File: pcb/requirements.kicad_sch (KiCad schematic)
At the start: 4 parts

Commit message: Updated worksheet template and logo
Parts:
- removed LOGO1: ~, CRGM Logos:FNWW Face 10mm, symbol CRGM Logos:FNWW Face
- added LOGO1: ~, CRGM Logos:CRGM Logo 5mm, symbol CRGM Logos:CRGM Logo
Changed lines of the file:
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@@
+	)
+	(symbol
+		(lib_id "CRGM Logos:CRGM Logo")
+		(at 245.11 173.99 0)
+		(unit 1)
+		(exclude_from_sim no)
+		(in_bom yes)
+		(on_board yes)
+		(dnp no)
+		(property "Reference" "LOGO1"
+			(at 245.11 185.674 0)
+			(effects
+				(font
+					(size 1.27 1.27)
+				)
+				(hide yes)
+			)
+		)
+		(property "Value" "~"
+			(at 245.11 173.99 0)
+			(effects
+				(font
+					(size 1.27 1.27)
+				)
+			)
+		)
+		(property "Footprint" "CRGM Logos:CRGM Logo 5mm"
+			(at 245.11 187.452 0)
+			(effects
+				(font
+					(size 1.27 1.27)
+				)
+				(hide yes)
+			)
+		)
+		(property "Datasheet" ""
+			(at 245.11 173.99 0)
+			(effects
+				(font
+					(size 1.27 1.27)
+				)
+				(hide yes)
+			)
+		)
+		(property "Description" ""
+			(at 245.11 173.99 0)
+			(effects
+				(font
+					(size 1.27 1.27)
+				)
+				(hide yes)
+			)
+		)
+		(property "LCSC" ""
+			(at 245.11 173.99 0)
+			(effects
+				(font
+					(size 1.27 1.27)
+				)
+				(hide yes)
+			)
+		)
+		(property "Digikey" ""
+			(at 245.11 173.99 0)
+			(effects
+				(font
+					(size 1.27 1.27)
+				)
+				(hide yes)
+			)
+		)
+		(property "Mouser" ""
+			(at 245.11 173.99 0)
+			(effects
+				(font
+					(size 1.27 1.27)
+				)
+				(hide yes)
+			)
+		)
+		(instances
+			(project ""
+				(path "/39407804-2746-45a9-a901-1039a9921518/2e166321-b713-45e0-87cf-342f1811c390"
+					(reference "LOGO1")
+					(unit 1)
+				)
+			)
+		)
 	)
 	(symbol
@@
 					(unit 1)
 				)
-			)
-		)
-	)
-	(symbol
-		(lib_id "CRGM Logos:FNWW Face")
-		(at 246.38 173.99 0)
-		(unit 1)
-		(exclude_from_sim no)
-		(in_bom no)
-		(on_board yes)
-		(dnp no)
-		(fields_autoplaced yes)
-		(property "Reference" "LOGO1"
-			(at 246.38 175.006 0)
-			(effects
-				(font
-					(size 1.27 1.27)
-				)
-				(hide yes)
-			)
-		)
-		(property "Value" "~"
-			(at 243.84 169.164 0)
-			(effects
-				(font
-					(size 1.27 1.27)
-				)
-				(hide yes)
-			)
-		)
-		(property "Footprint" "CRGM Logos:FNWW Face 10mm"
-			(at 246.38 183.134 0)
-			(effects
-				(font
-					(size 1.27 1.27)
-				)
-				(hide yes)
-			)
-		)
-		(property "Datasheet" ""
-			(at 243.84 169.164 0)
-			(effects
-				(font
-					(size 1.27 1.27)
-				)
-				(hide yes)
-			)
-		)
-		(property "Description" ""
-			(at 243.84 169.164 0)
-			(effects
-				(font
-					(size 1.27 1.27)
-				)
-				(hide yes)
-			)
-		)
-		(property "LCSC" ""
-			(at 246.38 173.99 0)
-			(effects
-				(font
-					(size 1.27 1.27)
-				)
-				(hide yes)
-			)
-		)
-		(property "Digikey" ""
-			(at 246.38 173.99 0)
-			(effects
-				(font
-					(size 1.27 1.27)
-				)
-				(hide yes)
-			)
-		)
-		(property "Mouser" ""
-			(at 246.38 173.99 0)
-			(effects
-				(font
-					(size 1.27 1.27)
-				)
-				(hide yes)
-			)
-		)
-		(instances
-			(project ""
-				(path "/39407804-2746-45a9-a901-1039a9921518/2e166321-b713-45e0-87cf-342f1811c390"
-					(reference "LOGO1")
-					(unit 1)
-				)

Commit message: Fixed footprint for Buzzer, XFC, USB ESD, and Power Switcher
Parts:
- LOGO1: now left out of the parts list
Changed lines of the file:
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@@
 		(unit 1)
 		(exclude_from_sim no)
-		(in_bom yes)
+		(in_bom no)
 		(on_board yes)
 		(dnp no)

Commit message: Change name in schematic
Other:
- title: Node Hardware -> Hub Hardware
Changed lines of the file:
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@@
 	(paper "A4")
 	(title_block
-		(title "Node Hardware")
+		(title "Hub Hardware")
 		(date "<<release-date>>")
 		(rev "<<tag>>")

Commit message: Adjusting for consistency
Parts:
- added H1, H2, H3, H4: ~, CRGM Mechanical:MountingHole_3.2mm_M3_Pad_Via, symbol Mechanical:MountingHole
- added LOGO5, LOGO6: ~, CRGM Logos:Roxy 5mm, symbol CRGM Logos:Roxy Logo
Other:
- note added: "Mechanical"
- title: Hub Hardware -> Aquarius Hub

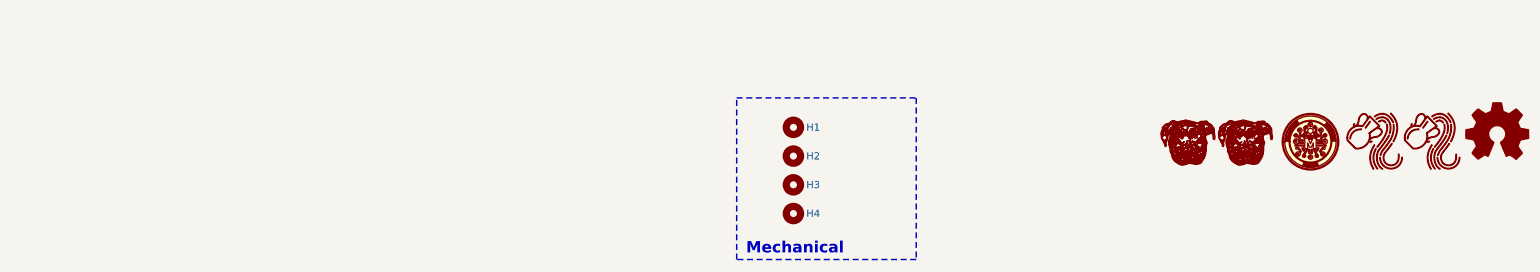
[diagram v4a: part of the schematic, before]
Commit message: Sync symbols and footprints
Transitioned to CRGM footprints
Added dimensions
Fixed some spacing
Adjusted properties
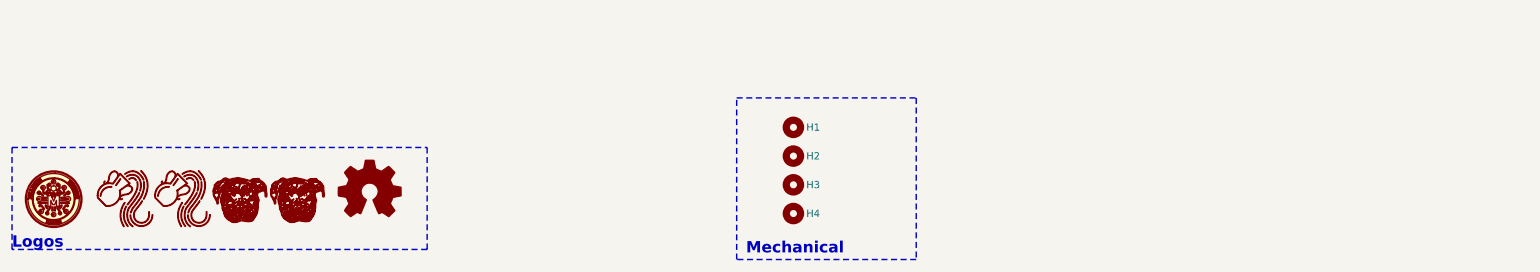
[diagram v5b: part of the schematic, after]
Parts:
- LOGO1: footprint CRGM Logos:CRGM Logo 5mm -> CRGM Logos:CRGM Logo 7mm; now in the parts list
- LOGO2: footprint CRGM Logos:Aquarius Logo 10mm -> CRGM Logos:Aquarius Logo 5mm
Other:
- note added: "Logos"
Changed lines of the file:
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@@
+		)
+	)
+	(rectangle
+		(start 15.494 175.006)
+		(end 88.9 193.04)
+		(stroke
+			(width 0.254)
+			(type dash)
+			(color 255 153 0 1)
+		)
+		(fill
+			(type none)
 		)
 	)
@@
 			)
 			(justify left top)
+		)
+	)
+	(text "Logos"
+		(exclude_from_sim no)
+		(at 15.494 193.04 0)
+		(effects
+			(font
+				(size 2 2)
+				(thickness 0.4)
+				(bold yes)
+			)
+			(justify left bottom)
 		)
 	)
@@
 	(symbol
 		(lib_id "CRGM Logos:CRGM Logo")
-		(at 245.11 173.99 0)
+		(at 22.86 184.15 0)
 		(unit 1)
 		(exclude_from_sim no)
-		(in_bom no)
+		(in_bom yes)
 		(on_board yes)
 		(dnp no)
 		(property "Reference" "LOGO1"
-			(at 245.11 185.674 0)
+			(at 22.86 195.834 0)
 			(effects
 				(font
@@
 		)
 		(property "Value" "~"
-			(at 245.11 173.99 0)
-			(effects
-				(font
-					(size 1.27 1.27)
-				)
-			)
-		)
-		(property "Footprint" "CRGM Logos:CRGM Logo 5mm"
-			(at 245.11 187.452 0)
+			(at 22.86 184.15 0)
+			(effects
+				(font
+					(size 1.27 1.27)
+				)
+				(hide yes)
+			)
+		)
+		(property "Footprint" "CRGM Logos:CRGM Logo 7mm"
+			(at 22.86 192.278 0)
 			(effects
 				(font
@@
 		)
 		(property "Datasheet" ""
-			(at 245.11 173.99 0)
+			(at 22.86 184.15 0)
 			(effects
 				(font
@@
 		)
 		(property "Description" ""
-			(at 245.11 173.99 0)
-			(effects
-				(font
-					(size 1.27 1.27)
-				)
-				(hide yes)
-			)
-		)
-		(property "LCSC" ""
-			(at 245.11 173.99 0)
-			(effects
-				(font
-					(size 1.27 1.27)
-				)
-				(hide yes)
-			)
-		)
-		(property "Digikey" ""
-			(at 245.11 173.99 0)
-			(effects
-				(font
-					(size 1.27 1.27)
-				)
-				(hide yes)
-			)
-		)
-		(property "Mouser" ""
-			(at 245.11 173.99 0)
+			(at 22.86 184.15 0)
 			(effects
 				(font
@@
 	(symbol
 		(lib_id "Graphic:Logo_Open_Hardware_Small")
-		(at 278.13 172.72 0)
+		(at 78.74 182.88 0)
 		(unit 1)
 		(exclude_from_sim no)
@@
 		(dnp no)
 		(property "Reference" "LOGO3"
-			(at 278.13 165.735 0)
+			(at 78.74 175.895 0)
 			(effects
 				(font
@@
 		)
 		(property "Value" "~"
-			(at 278.13 178.435 0)
+			(at 78.74 188.595 0)
 			(effects
 				(font
@@
 		)
 		(property "Footprint" "Symbol:OSHW-Logo_5.7x6mm_SilkScreen"
-			(at 278.13 172.72 0)
+			(at 78.74 182.88 0)
 			(effects
 				(font
@@
 		)
 		(property "Datasheet" "~"
-			(at 278.13 172.72 0)
+			(at 78.74 182.88 0)
 			(effects
 				(font
@@
 		)
 		(property "Description" ""
-			(at 278.13 172.72 0)
+			(at 78.74 182.88 0)
 			(effects
 				(font
@@
 		)
 		(property "LCSC" ""
-			(at 278.13 172.72 0)
+			(at 78.74 182.88 0)
 			(effects
 				(font
@@
 		)
 		(property "Digikey" ""
-			(at 278.13 172.72 0)
+			(at 78.74 182.88 0)
 			(effects
 				(font
@@
 		)
 		(property "Mouser" ""
-			(at 278.13 172.72 0)
+			(at 78.74 182.88 0)
 			(effects
 				(font
@@
 	(symbol
 		(lib_id "CRGM Logos:Roxy Logo")
-		(at 223.52 173.99 0)
+		(at 55.88 184.15 0)
 		(unit 1)
 		(exclude_from_sim no)
@@
 		(dnp no)
 		(property "Reference" "LOGO5"
-			(at 223.52 180.34 0)
+			(at 55.88 190.5 0)
 			(effects
 				(font
@@
 		)
 		(property "Value" "~"
-			(at 223.52 173.99 0)
-			(effects
-				(font
-					(size 1.27 1.27)
-				)
+			(at 55.88 184.15 0)
+			(effects
+				(font
+					(size 1.27 1.27)
+				)
+				(hide yes)
 			)
 		)
 		(property "Footprint" "CRGM Logos:Roxy 5mm"
-			(at 223.52 182.118 0)
+			(at 55.88 192.278 0)
 			(effects
 				(font
@@
 		)
 		(property "Datasheet" ""
-			(at 223.52 173.99 0)
+			(at 55.88 184.15 0)
 			(effects
 				(font
@@
 		)
 		(property "Description" ""
-			(at 223.52 173.99 0)
+			(at 55.88 184.15 0)
 			(effects
 				(font
@@
 		)
 		(property "LCSC" ""
-			(at 223.52 173.99 0)
+			(at 55.88 184.15 0)
 			(effects
 				(font
@@
 		)
 		(property "Digikey" ""
-			(at 223.52 173.99 0)
+			(at 55.88 184.15 0)
 			(effects
 				(font
@@
 		)
 		(property "Mouser" ""
-			(at 223.52 173.99 0)
+			(at 55.88 184.15 0)
 			(effects
 				(font
@@
 	(symbol
 		(lib_id "CRGM Logos:Aquarius Logo")
-		(at 266.7 173.99 0)
+		(at 45.72 184.15 0)
 		(unit 1)
 		(exclude_from_sim no)
@@
 		(fields_autoplaced yes)
 		(property "Reference" "LOGO4"
-			(at 266.954 175.26 0)
+			(at 45.974 185.42 0)
 			(effects
 				(font
@@
 		)
 		(property "Value" "~"
-			(at 264.414 168.91 0)
+			(at 43.434 179.07 0)
 			(effects
 				(font
@@
 		)
 		(property "Footprint" "CRGM Logos:Aquarius Logo 5mm"
-			(at 268.986 181.864 0)
+			(at 48.006 192.024 0)
 			(effects
 				(font
@@
 		)
 		(property "Datasheet" ""
-			(at 264.414 168.91 0)
+			(at 43.434 179.07 0)
 			(effects
 				(font
@@
 		)
 		(property "Description" ""
-			(at 264.414 168.91 0)
+			(at 43.434 179.07 0)
+			(effects
+				(font
+					(size 1.27 1.27)
+				)
+				(hide yes)
+			)
+		)
+		(property "LCSC" ""
+			(at 45.72 184.15 0)
+			(effects
+				(font
+					(size 1.27 1.27)
+				)
+				(hide yes)
+			)
+		)
+		(property "Digikey" ""
+			(at 45.72 184.15 0)
+			(effects
+				(font
+					(size 1.27 1.27)
+				)
+				(hide yes)
+			)
+		)
+		(property "Mouser" ""
+			(at 45.72 184.15 0)
 			(effects
 				(font
@@
 	(symbol
 		(lib_id "CRGM Logos:Aquarius Logo")
-		(at 256.54 173.99 0)
+		(at 35.56 184.15 0)
 		(unit 1)
 		(exclude_from_sim no)
@@
 		(fields_autoplaced yes)
 		(property "Reference" "LOGO2"
-			(at 256.794 175.26 0)
+			(at 35.814 185.42 0)
 			(effects
 				(font
@@
 		)
 		(property "Value" "~"
-			(at 254.254 168.91 0)
-			(effects
-				(font
-					(size 1.27 1.27)
-				)
-				(hide yes)
-			)
-		)
-		(property "Footprint" "CRGM Logos:Aquarius Logo 10mm"
-			(at 258.826 181.864 0)
+			(at 33.274 179.07 0)
+			(effects
+				(font
+					(size 1.27 1.27)
+				)
+				(hide yes)
+			)
+		)
+		(property "Footprint" "CRGM Logos:Aquarius Logo 5mm"
+			(at 37.846 192.024 0)
 			(effects
 				(font
@@
 		)
 		(property "Datasheet" ""
-			(at 254.254 168.91 0)
+			(at 33.274 179.07 0)
 			(effects
 				(font
@@
 		)
 		(property "Description" ""
-			(at 254.254 168.91 0)
+			(at 33.274 179.07 0)
 			(effects
 				(font
@@
 		)
 		(property "LCSC" ""
-			(at 256.54 173.99 0)
+			(at 35.56 184.15 0)
 			(effects
 				(font
@@
 		)
 		(property "Digikey" ""
-			(at 256.54 173.99 0)
+			(at 35.56 184.15 0)
 			(effects
 				(font
@@
 		)
 		(property "Mouser" ""
-			(at 256.54 173.99 0)
+			(at 35.56 184.15 0)
 			(effects
 				(font
@@
 	(symbol
 		(lib_id "CRGM Logos:Roxy Logo")
-		(at 233.68 173.99 0)
+		(at 66.04 184.15 0)
 		(unit 1)
 		(exclude_from_sim no)
@@
 		(dnp no)
 		(property "Reference" "LOGO6"
-			(at 233.68 180.34 0)
+			(at 66.04 190.5 0)
 			(effects
 				(font
@@
 		)
 		(property "Value" "~"
-			(at 233.68 173.99 0)
-			(effects
-				(font
-					(size 1.27 1.27)
-				)
+			(at 66.04 184.15 0)
+			(effects
+				(font
+					(size 1.27 1.27)
+				)
+				(hide yes)
 			)
 		)
 		(property "Footprint" "CRGM Logos:Roxy 5mm"
-			(at 233.68 182.118 0)
+			(at 66.04 192.278 0)
 			(effects
 				(font
@@
 		)
 		(property "Datasheet" ""
-			(at 233.68 173.99 0)
+			(at 66.04 184.15 0)
 			(effects
 				(font
@@
 		)
 		(property "Description" ""
-			(at 233.68 173.99 0)
+			(at 66.04 184.15 0)
 			(effects
 				(font
@@
 		)
 		(property "LCSC" ""
-			(at 233.68 173.99 0)
+			(at 66.04 184.15 0)
 			(effects
 				(font
@@
 		)
 		(property "Digikey" ""
-			(at 233.68 173.99 0)
+			(at 66.04 184.15 0)
 			(effects
 				(font
@@
 		)
 		(property "Mouser" ""
-			(at 233.68 173.99 0)
-			(effects
-				(font
+			(at 66.04 184.15 0)
+			(effects
+				(font

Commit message: Clean up and consistency
Moved buzzer to MCU
Fixed model directory
Set font size
Set outline size
Upscaled Roxy ❤️
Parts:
- LOGO5, LOGO6: footprint CRGM Logos:Roxy 5mm -> CRGM Logos:Roxy 6.5mm
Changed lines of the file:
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@@
 			)
 		)
-		(property "Footprint" "CRGM Logos:Roxy 5mm"
+		(property "Footprint" "CRGM Logos:Roxy 6.5mm"
 			(at 55.88 192.278 0)
 			(effects
@@
 			)
 		)
-		(property "Footprint" "CRGM Logos:Roxy 5mm"
+		(property "Footprint" "CRGM Logos:Roxy 6.5mm"
 			(at 66.04 192.278 0)
 			(effects
